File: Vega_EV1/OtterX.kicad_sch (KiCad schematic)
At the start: 62 parts, among them J1 VERA_CONN, J11 KMDGX-6SG, J12 VIA1 Extra Pins, J17 SNES23, J18 SNES0, J19 SNES1, J2 VIA2 Header, J29 AudioPlug3, J3 IEC, J9 I2C, U1 W65C02S, U11 74ACT163, U2 W65C22S, X1 ACH-16.000MHZ-EK

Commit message: Misc layout fixes.
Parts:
- J12: footprint Connector_PinHeader_2.54mm:PinHeader_2x04_P2.54mm_Vertical -> Connector_PinSocket_2.54mm:PinSocket_2x04_P2.54mm_Horizontal
- J17: footprint Connector_PinSocket_2.54mm:PinSocket_2x03_P2.54mm_Vertical -> Connector_PinSocket_2.54mm:PinSocket_2x03_P2.54mm_Horizontal
- J3: footprint Connector_PinHeader_2.54mm:PinHeader_2x05_P2.54mm_Vertical -> Connector_PinSocket_2.54mm:PinSocket_2x05_P2.54mm_Vertical
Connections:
- net +5V: now also J12.7 (Pin_7); no longer J12.1 (Pin_1)
- net CA1: now also J12.8 (Pin_8); no longer J12.2 (Pin_2)
- net CA2: now also J12.6 (Pin_6); no longer J12.4 (Pin_4)
- net CB2: now also J12.4 (Pin_4); no longer J12.6 (Pin_6)
- net GND: now also J12.2 (Pin_2); no longer J12.8 (Pin_8)
- net V1PB0: now also J12.5 (Pin_5); no longer J12.3 (Pin_3)
- net V1PB1: now also J12.3 (Pin_3); no longer J12.5 (Pin_5)
- net V1PB2: now also J12.1 (Pin_1); no longer J12.7 (Pin_7)
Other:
- moved on the sheet: J12
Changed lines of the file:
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@@
 	(global_label "CA1"
 		(shape output)
-		(at 313.055 90.17 0)
+		(at 312.42 90.17 0)
 		(fields_autoplaced yes)
 		(effects
@@
 		)
 		(property "Intersheetrefs" "${INTERSHEET_REFS}"
-			(at 319.5289 90.17 0)
+			(at 318.8939 90.17 0)
 			(effects
 				(font
@@
 	(global_label "CB2"
 		(shape output)
-		(at 313.055 95.25 0)
+		(at 312.42 95.25 0)
 		(fields_autoplaced yes)
 		(effects
@@
 		)
 		(property "Intersheetrefs" "${INTERSHEET_REFS}"
-			(at 319.2176 95.1706 0)
+			(at 318.5826 95.1706 0)
 			(effects
 				(font
@@
 	(global_label "CA2"
 		(shape output)
-		(at 313.055 92.71 0)
+		(at 312.42 92.71 0)
 		(fields_autoplaced yes)
 		(effects
@@
 		)
 		(property "Intersheetrefs" "${INTERSHEET_REFS}"
-			(at 319.5289 92.71 0)
+			(at 318.8939 92.71 0)
 			(effects
 				(font
@@
 	(global_label "V1PB0"
 		(shape bidirectional)
-		(at 300.355 92.71 180)
+		(at 299.72 92.71 180)
 		(fields_autoplaced yes)
 		(effects
@@
 		)
 		(property "Intersheetrefs" "${INTERSHEET_REFS}"
-			(at 291.8943 92.6306 0)
+			(at 291.2593 92.6306 0)
 			(effects
 				(font
@@
 	(global_label "V1PB2"
 		(shape bidirectional)
-		(at 300.355 97.79 180)
+		(at 299.72 97.79 180)
 		(fields_autoplaced yes)
 		(effects
@@
 		)
 		(property "Intersheetrefs" "${INTERSHEET_REFS}"
-			(at 291.8943 97.7106 0)
+			(at 291.2593 97.7106 0)
 			(effects
 				(font
@@
 	(global_label "V1PB1"
 		(shape bidirectional)
-		(at 300.355 95.25 180)
+		(at 299.72 95.25 180)
 		(fields_autoplaced yes)
 		(effects
@@
 		)
 		(property "Intersheetrefs" "${INTERSHEET_REFS}"
-			(at 291.8943 95.1706 0)
+			(at 291.2593 95.1706 0)
 			(effects
 				(font
@@
 	(symbol
 		(lib_id "power:GND")
-		(at 313.055 97.79 0)
+		(at 312.42 97.79 0)
 		(mirror y)
 		(unit 1)
@@
 		(fields_autoplaced yes)
 		(property "Reference" "#PWR010"
-			(at 313.055 104.14 0)
+			(at 312.42 104.14 0)
 			(effects
 				(font
@@
 		)
 		(property "Value" "GND"
-			(at 313.055 102.235 0)
+			(at 312.42 102.235 0)
 			(effects
 				(font
@@
 		)
 		(property "Footprint" ""
-			(at 313.055 97.79 0)
+			(at 312.42 97.79 0)
 			(effects
 				(font
@@
 		)
 		(property "Datasheet" ""
-			(at 313.055 97.79 0)
+			(at 312.42 97.79 0)
 			(effects
 				(font
@@
 		)
 		(property "Description" "Power symbol creates a global label with name \"GND\" , ground"
-			(at 313.055 97.79 0)
+			(at 312.42 97.79 0)
 			(effects
 				(font
@@
 	(symbol
 		(lib_id "power:+5V")
-		(at 300.355 90.17 90)
+		(at 299.72 90.17 90)
 		(mirror x)
 		(unit 1)
@@
 		(fields_autoplaced yes)
 		(property "Reference" "#PWR09"
-			(at 304.165 90.17 0)
+			(at 303.53 90.17 0)
 			(effects
 				(font
@@
 		)
 		(property "Value" "+5V"
-			(at 296.545 90.1699 90)
+			(at 295.91 90.1699 90)
 			(effects
 				(font
@@
 		)
 		(property "Footprint" ""
-			(at 300.355 90.17 0)
+			(at 299.72 90.17 0)
 			(effects
 				(font
@@
 		)
 		(property "Datasheet" ""
-			(at 300.355 90.17 0)
+			(at 299.72 90.17 0)
 			(effects
 				(font
@@
 		)
 		(property "Description" "Power symbol creates a global label with name \"+5V\""
-			(at 300.355 90.17 0)
+			(at 299.72 90.17 0)
 			(effects
 				(font
@@
 		(on_board yes)
 		(dnp no)
-		(fields_autoplaced yes)
 		(property "Reference" "J3"
 			(at 307.34 133.35 0)
@@
 			)
 		)
-		(property "Footprint" "Connector_PinHeader_2.54mm:PinHeader_2x05_P2.54mm_Vertical"
+		(property "Footprint" "Connector_PinSocket_2.54mm:PinSocket_2x05_P2.54mm_Vertical"
 			(at 306.07 144.78 0)
 			(effects
@@
 	(symbol
 		(lib_id "Connector_Generic:Conn_02x04_Odd_Even")
-		(at 305.435 92.71 0)
+		(at 304.8 95.25 0)
+		(mirror x)
 		(unit 1)
 		(exclude_from_sim no)
@@
 		(on_board yes)
 		(dnp no)
-		(fields_autoplaced yes)
 		(property "Reference" "J12"
-			(at 306.705 83.82 0)
+			(at 306.07 104.14 0)
 			(effects
 				(font
@@
 		)
 		(property "Value" "VIA1 Extra Pins"
-			(at 306.705 86.36 0)
+			(at 306.07 101.6 0)
 			(effects
 				(font
@@
 			)
 		)
-		(property "Footprint" "Connector_PinHeader_2.54mm:PinHeader_2x04_P2.54mm_Vertical"
-			(at 305.435 92.71 0)
+		(property "Footprint" "Connector_PinSocket_2.54mm:PinSocket_2x04_P2.54mm_Horizontal"
+			(at 304.8 95.25 0)
 			(effects
 				(font
@@
 		)
 		(property "Datasheet" "~"
-			(at 305.435 92.71 0)
+			(at 304.8 95.25 0)
 			(effects
 				(font
@@
 		)
 		(property "Description" ""
-			(at 305.435 92.71 0)
+			(at 304.8 95.25 0)
 			(effects
 				(font
@@
 			)
 		)
-		(property "Footprint" "Connector_PinSocket_2.54mm:PinSocket_2x03_P2.54mm_Vertical"
+		(property "Footprint" "Connector_PinSocket_2.54mm:PinSocket_2x03_P2.54mm_Horizontal"
 			(at 155.575 229.87 0)
 			(effects

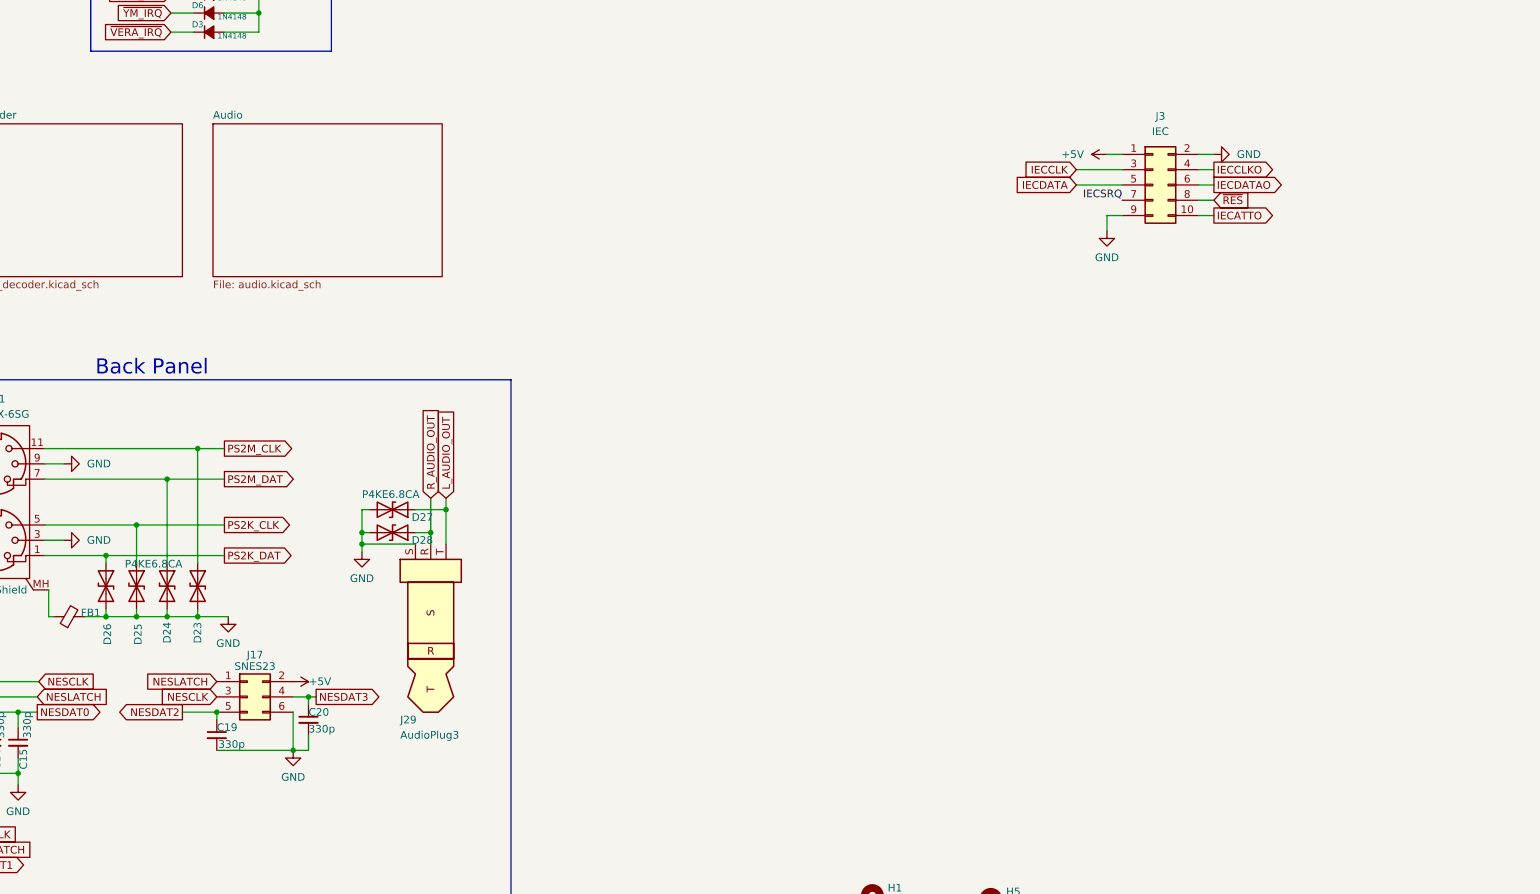
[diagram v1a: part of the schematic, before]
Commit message: Add IEC circuit back in, without the port.
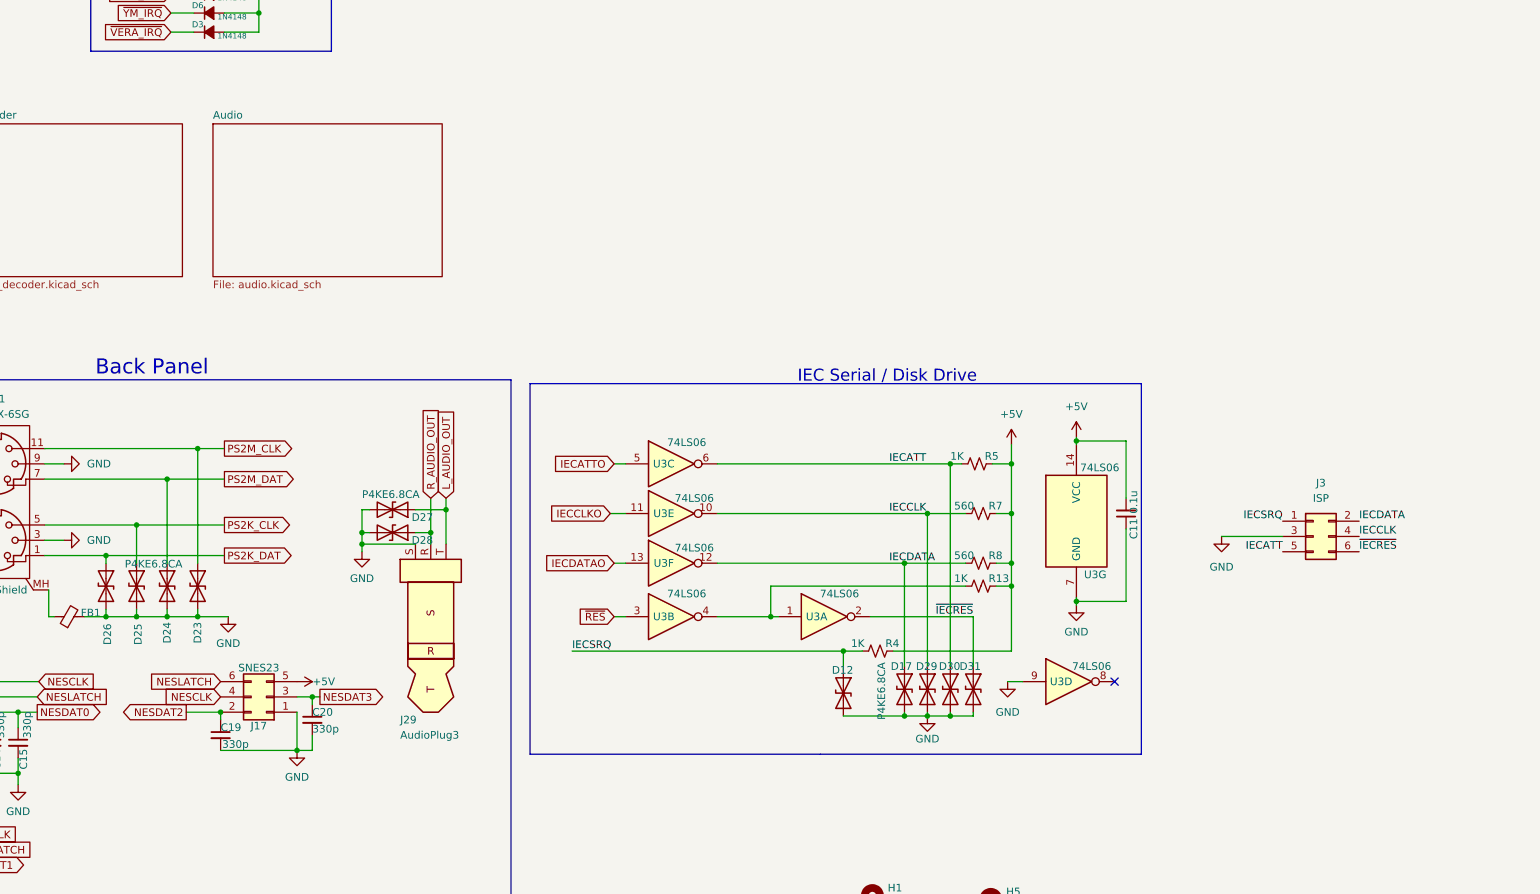
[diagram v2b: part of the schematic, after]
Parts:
- removed J3: IEC, Connector_PinSocket_2.54mm:PinSocket_2x05_P2.54mm_Vertical, symbol Connector_Generic:Conn_02x05_Odd_Even
- added C11: 0.1u, Capacitor_THT:C_Disc_D4.3mm_W1.9mm_P5.00mm, symbol Device:C_Small
- added D12, D17, D29, D30, D31: P4KE6.8CA, Diode_THT:D_DO-41_SOD81_P7.62mm_Horizontal, symbol Device:D_TVS
- added J3: ISP, Connector_IDC:IDC-Header_2x03_P2.54mm_Vertical, symbol Connector_Generic:Conn_02x03_Odd_Even
- added R13, R4, R5: 1K, Resistor_THT:R_Axial_DIN0207_L6.3mm_D2.5mm_P7.62mm_Horizontal, symbol Device:R_Small_US
- added R7, R8: 560, Resistor_THT:R_Axial_DIN0207_L6.3mm_D2.5mm_P7.62mm_Horizontal, symbol Device:R_Small_US
- added U3: 74LS06, OtterX:DIP-14_W7.62mm_ShortWidePads, symbol 74xx:74LS06
- J12: footprint Connector_PinSocket_2.54mm:PinSocket_2x04_P2.54mm_Horizontal -> Connector_PinSocket_2.54mm:PinSocket_2x04_P2.54mm_Vertical
- J17: footprint Connector_PinSocket_2.54mm:PinSocket_2x03_P2.54mm_Horizontal -> Connector_IDC:IDC-Header_2x03_P2.54mm_Vertical
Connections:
- net +5V: now also J17.5 (Pin_5), C11.2, R13.1, R4.1, R5.1, R7.1, R8.1, U3.14 (VCC); no longer J17.2 (Pin_2)
- net GND: now also J17.1 (Pin_1), C11.1, D12.2 (A2), D17.2 (A2), D29.2 (A2), D30.2 (A2), D31.2 (A2), J3.3 (Pin_3), U3.7 (GND), U3.9; no longer J17.6 (Pin_6)
- net IECATTO: now also U3.5
- net IECCLK: now also D29.1 (A1), J3.4 (Pin_4), R7.2, U3.10
- net IECCLKO: now also U3.11
- net IECDATA: now also D17.1 (A1), J3.2 (Pin_2), R8.2, U3.12
- net IECDATAO: now also U3.13
- net IECSRQ: now also D12.1 (A1), J3.1 (Pin_1), R4.2
- net NESCLK: now also J17.4 (Pin_4); no longer J17.3 (Pin_3)
- net NESDAT2: now also J17.2 (Pin_2); no longer J17.5 (Pin_5)
- net NESDAT3: now also J17.3 (Pin_3); no longer J17.4 (Pin_4)
- net NESLATCH: now also J17.6 (Pin_6); no longer J17.1 (Pin_1)
- net ~{RES}: now also U3.3
- new net: R13.2, U3.1, U3.4
- new net IECATT: D30.1 (A1), J3.5 (Pin_5), R5.2, U3.6
- new net ~{IECRES}: D31.1 (A1), J3.6 (Pin_6), U3.2
- no-connect marks 11 -> 12
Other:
- note added: "IEC Serial / Disk Drive"
- moved on the sheet: C19, C20, J17
